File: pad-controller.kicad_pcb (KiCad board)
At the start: 2 copper layers, 14 parts, among them M1 Motor_Servo, M2 Motor_Servo, M3 Motor_Servo, M4 Motor_Servo, SW1 SW_Push_Dual, U2 TPS56121, U3 LD1117S33TR_SOT223

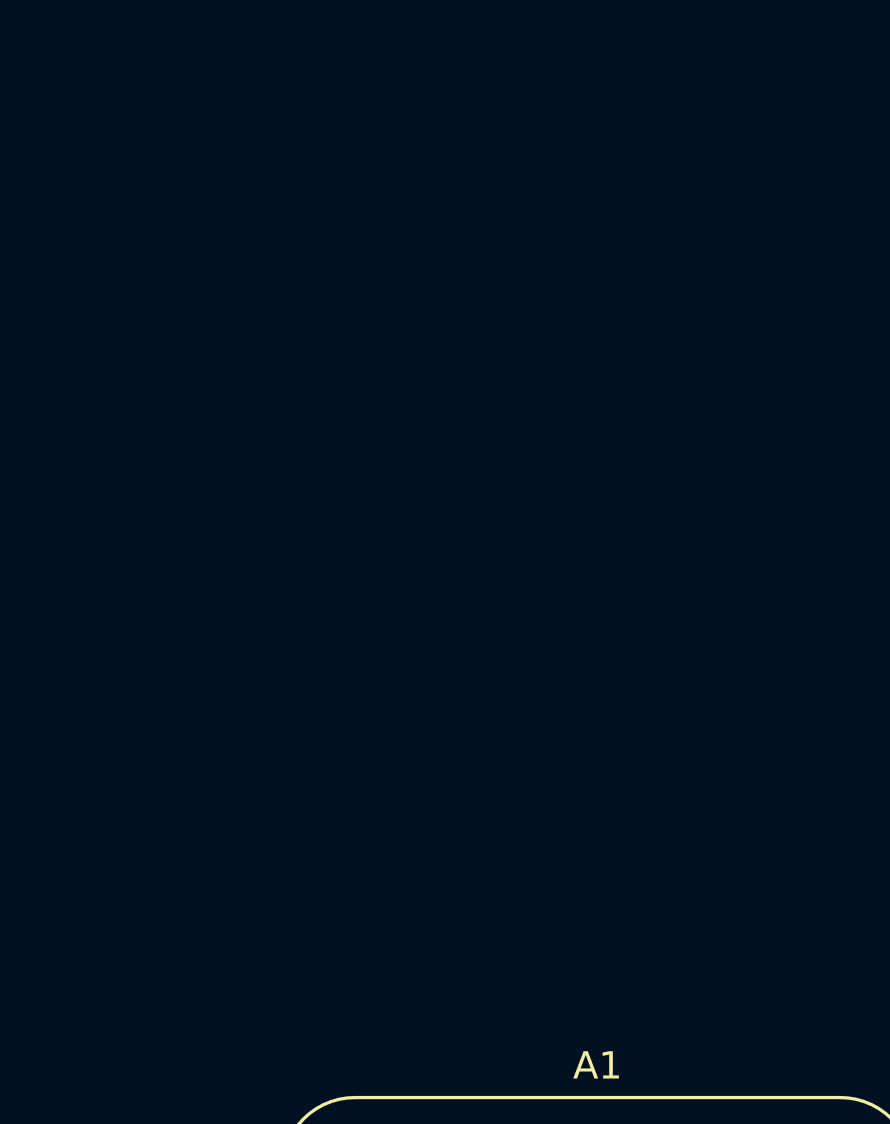
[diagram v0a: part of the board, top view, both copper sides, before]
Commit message: Add XBee footprint
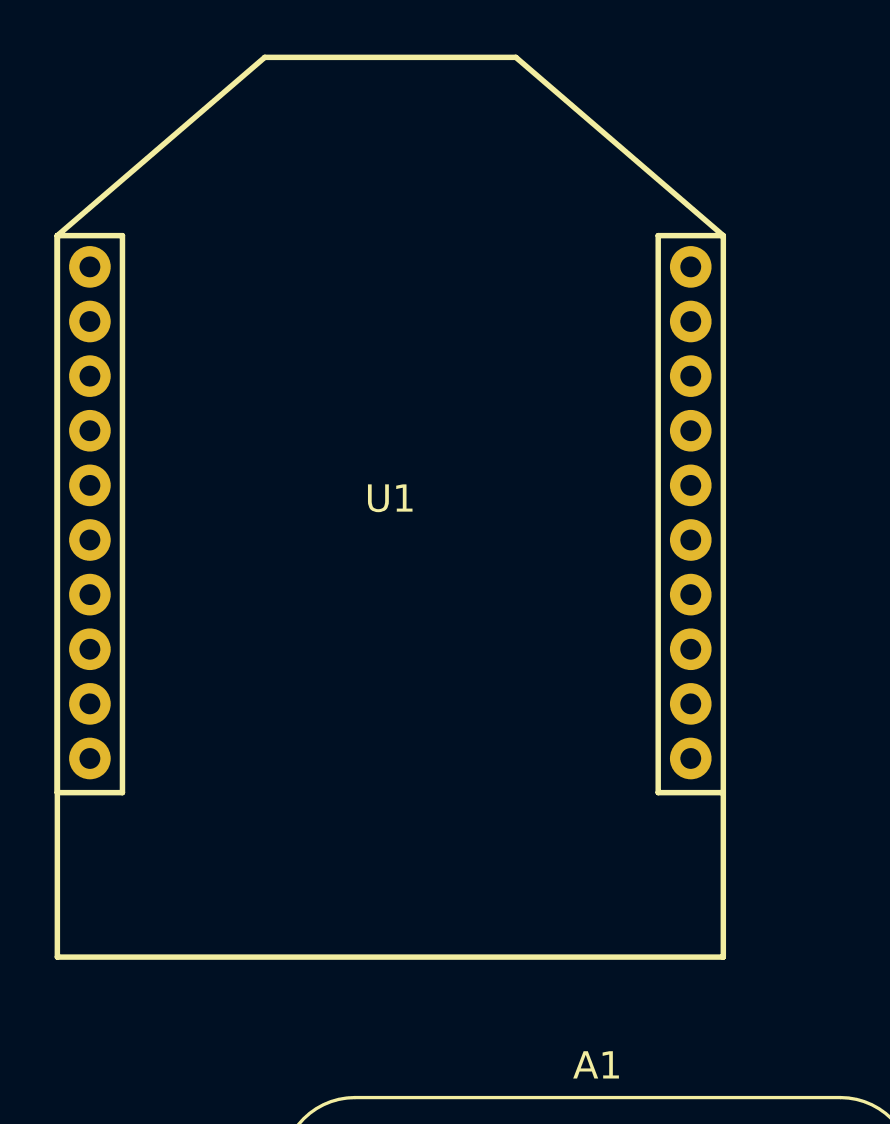
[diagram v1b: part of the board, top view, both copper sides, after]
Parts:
- added U1: Xbee, Marks_Footprints:XBee-PRO 900HP, F.Cu at (65.2, 49.4)
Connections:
- A1 pad 10: unconnected-(A1-A5-Pad10) -> Break Wire
- A1 pad 9: unconnected-(A1-A4-Pad9) -> E-Match
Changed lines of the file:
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@@
   (net 7 "unconnected-(A1-A2-Pad7)")
   (net 8 "unconnected-(A1-A3-Pad8)")
-  (net 9 "unconnected-(A1-A4-Pad9)")
-  (net 10 "unconnected-(A1-A5-Pad10)")
+  (net 9 "E-Match")
+  (net 10 "unconnected-(U1-DIO12{slash}SPI_MISO-Pad4)")
   (net 11 "unconnected-(A1-SCK-Pad11)")
   (net 12 "unconnected-(A1-MOSI-Pad12)")
@@
   (net 41 "Net-(U2-PGOOD)")
   (net 42 "+6V")
+  (net 43 "unconnected-(U1-DIO10{slash}PWM0-Pad6)")
+  (net 44 "unconnected-(U1-DIO11{slash}PWM1-Pad7)")
+  (net 45 "unconnected-(U1-Reserved-Pad8)")
+  (net 46 "unconnected-(U1-DIO4{slash}SPI_MOSI-Pad11)")
+  (net 47 "unconnected-(U1-CTS{slash}DIO7-Pad12)")
+  (net 48 "unconnected-(U1-ON_SLEEP{slash}DIO9-Pad13)")
+  (net 49 "unconnected-(U1-Associate{slash}DIO5-Pad15)")
+  (net 50 "unconnected-(U1-AD3{slash}DIO3{slash}SPI_SSEL-Pad17)")
+  (net 51 "unconnected-(U1-AD2{slash}DIO{slash}SPI_CLK-Pad18)")
+  (net 52 "unconnected-(U1-AD1{slash}DIO1{slash}SPI_ATTN-Pad19)")
+  (net 53 "unconnected-(U1-AD0{slash}DIO0-Pad20)")
   (footprint "Module:Adafruit_Feather" (layer "F.Cu")
     (at 62.63 77.295)
@@
       (net 8 "unconnected-(A1-A3-Pad8)") (pinfunction "A3") (pintype "bidirectional"))
     (pad "9" thru_hole circle (at 0 20.32 180) (size 1.6 1.6) (drill 0.8) (layers "*.Cu" "*.Mask")
-      (net 9 "unconnected-(A1-A4-Pad9)") (pinfunction "A4") (pintype "bidirectional"))
+      (net 9 "E-Match") (pinfunction "A4") (pintype "bidirectional"))
     (pad "10" thru_hole circle (at 0 22.86 180) (size 1.6 1.6) (drill 0.8) (layers "*.Cu" "*.Mask")
-      (net 10 "unconnected-(A1-A5-Pad10)") (pinfunction "A5") (pintype "bidirectional"))
+      (net 23 "Break Wire") (pinfunction "A5") (pintype "bidirectional"))
     (pad "11" thru_hole circle (at 0 25.4 180) (size 1.6 1.6) (drill 0.8) (layers "*.Cu" "*.Mask")
       (net 11 "unconnected-(A1-SCK-Pad11)") (pinfunction "SCK") (pintype "bidirectional"))
@@
     )
   )
+  (footprint "Marks_Footprints:XBee-PRO 900HP" (layer "F.Cu")
+    (at 65.2 49.42)
+    (property "Description" "")
+    (property "Part No." "")
+    (property "Sheetfile" "pad-controller.kicad_sch")
+    (property "Sheetname" "")
+    (attr through_hole)
+    (fp_text reference "U1" (at 0 -0.5 unlocked) (layer "F.SilkS")
+        (effects (font (size 1 1) (thickness 0.1)))
+    )
+    (fp_text value "Xbee" (at 0 1 unlocked) (layer "F.Fab")
+        (effects (font (size 1 1) (thickness 0.15)))
+    )
+    (fp_text user "${REFERENCE}" (at 0 2.5 unlocked) (layer "F.Fab")
+        (effects (font (size 1 1) (thickness 0.15)))
+    )
+    (fp_line (start -12.192 -10.1441) (end -12.192 10.2503)
+      (stroke (width 0.2) (type solid)) (layer "F.SilkS"))
+    (fp_line (start -12.192 -10.1441) (end -9.808 -10.1441)
+      (stroke (width 0.2) (type solid)) (layer "F.SilkS"))
+    (fp_line (start -12.192 -10.1441) (end -4.5974 -16.6719)
+      (stroke (width 0.2) (type solid)) (layer "F.SilkS"))
+    (fp_line (start -12.192 10.2503) (end -9.808 10.2503)
+      (stroke (width 0.2) (type solid)) (layer "F.SilkS"))
+    (fp_line (start -12.192 16.2719) (end -12.192 -10.1441)
+      (stroke (width 0.2) (type solid)) (layer "F.SilkS"))
+    (fp_line (start -12.192 16.2719) (end 12.192 16.2719)
+      (stroke (width 0.2) (type solid)) (layer "F.SilkS"))
+    (fp_line (start -9.808 -10.1441) (end -9.808 10.2503)
+      (stroke (width 0.2) (type solid)) (layer "F.SilkS"))
+    (fp_line (start -4.5974 -16.6719) (end 4.5974 -16.6719)
+      (stroke (width 0.2) (type solid)) (layer "F.SilkS"))
+    (fp_line (start 9.808 -10.1441) (end 9.808 10.2503)
+      (stroke (width 0.2) (type solid)) (layer "F.SilkS"))
+    (fp_line (start 12.192 -10.1441) (end 4.5974 -16.6719)
+      (stroke (width 0.2) (type solid)) (layer "F.SilkS"))
+    (fp_line (start 12.192 -10.1441) (end 9.808 -10.1441)
+      (stroke (width 0.2) (type solid)) (layer "F.SilkS"))
+    (fp_line (start 12.192 10.2503) (end 9.808 10.2503)
+      (stroke (width 0.2) (type solid)) (layer "F.SilkS"))
+    (fp_line (start 12.192 16.2719) (end 12.192 -10.1441)
+      (stroke (width 0.2) (type solid)) (layer "F.SilkS"))
+    (pad "1" thru_hole circle (at -11 -9) (size 1.524 1.524) (drill 0.762) (layers "*.Cu" "*.Mask")
+      (net 2 "+3.3V") (pinfunction "VCC") (pintype "power_in"))
+    (pad "2" thru_hole circle (at -11 -7) (size 1.524 1.524) (drill 0.762) (layers "*.Cu" "*.Mask")
+      (net 14 "MCU RX") (pinfunction "DOUT/DIO13") (pintype "bidirectional"))
+    (pad "3" thru_hole circle (at -11 -5) (size 1.524 1.524) (drill 0.762) (layers "*.Cu" "*.Mask")
+      (net 15 "MCU TX") (pinfunction "DIN/CONFIG/DIO14") (pintype "bidirectional"))
+    (pad "4" thru_hole circle (at -11 -3) (size 1.524 1.524) (drill 0.762) (layers "*.Cu" "*.Mask")
+      (net 10 "unconnected-(U1-DIO12{slash}SPI_MISO-Pad4)") (pinfunction "DIO12/SPI_MISO") (pintype "bidirectional"))
+    (pad "5" thru_hole circle (at -11 -1) (size 1.524 1.524) (drill 0.762) (layers "*.Cu" "*.Mask")
+      (net 29 "/XBee Reset") (pinfunction "RESET") (pintype "input"))
+    (pad "6" thru_hole circle (at -11 1) (size 1.524 1.524) (drill 0.762) (layers "*.Cu" "*.Mask")
+      (net 43 "unconnected-(U1-DIO10{slash}PWM0-Pad6)") (pinfunction "DIO10/PWM0") (pintype "bidirectional"))
+    (pad "7" thru_hole circle (at -11 3) (size 1.524 1.524) (drill 0.762) (layers "*.Cu" "*.Mask")
+      (net 44 "unconnected-(U1-DIO11{slash}PWM1-Pad7)") (pinfunction "DIO11/PWM1") (pintype "bidirectional"))
+    (pad "8" thru_hole circle (at -11 5) (size 1.524 1.524) (drill 0.762) (layers "*.Cu" "*.Mask")
+      (net 45 "unconnected-(U1-Reserved-Pad8)") (pinfunction "Reserved") (pintype "unspecified"))
+    (pad "9" thru_hole circle (at -11 7) (size 1.524 1.524) (drill 0.762) (layers "*.Cu" "*.Mask")
+      (net 25 "XBee DTR") (pinfunction "DTR/SLEEP_RQ/DIO8") (pintype "bidirectional"))
+    (pad "10" thru_hole circle (at -11 9) (size 1.524 1.524) (drill 0.762) (layers "*.Cu" "*.Mask")
+      (net 4 "GND") (pinfunction "GND") (pintype "unspecified"))
+    (pad "11" thru_hole circle (at 11 9 180) (size 1.524 1.524) (drill 0.762) (layers "*.Cu" "*.Mask")
+      (net 46 "unconnected-(U1-DIO4{slash}SPI_MOSI-Pad11)") (pinfunction "DIO4/SPI_MOSI") (pintype "bidirectional"))
+    (pad "12" thru_hole circle (at 11 7 180) (size 1.524 1.524) (drill 0.762) (layers "*.Cu" "*.Mask")
+      (net 47 "unconnected-(U1-CTS{slash}DIO7-Pad12)") (pinfunction "CTS/DIO7") (pintype "bidirectional"))
+    (pad "13" thru_hole circle (at 11 5 180) (size 1.524 1.524) (drill 0.762) (layers "*.Cu" "*.Mask")
+      (net 48 "unconnected-(U1-ON_SLEEP{slash}DIO9-Pad13)") (pinfunction "ON_SLEEP/DIO9") (pintype "bidirectional"))
+    (pad "14" thru_hole circle (at 11 3 180) (size 1.524 1.524) (drill 0.762) (layers "*.Cu" "*.Mask")
+      (net 4 "GND") (pinfunction "VREF") (pintype "unspecified"))
+    (pad "15" thru_hole circle (at 11 1 180) (size 1.524 1.524) (drill 0.762) (layers "*.Cu" "*.Mask")
+      (net 49 "unconnected-(U1-Associate{slash}DIO5-Pad15)") (pinfunction "Associate/DIO5") (pintype "bidirectional"))
+    (pad "16" thru_hole circle (at 11 -1 180) (size 1.524 1.524) (drill 0.762) (layers "*.Cu" "*.Mask")
+      (net 24 "XBee RTS") (pinfunction "RTS/DIO6") (pintype "bidirectional"))
+    (pad "17" thru_hole circle (at 11 -3 180) (size 1.524 1.524) (drill 0.762) (layers "*.Cu" "*.Mask")
+      (net 50 "unconnected-(U1-AD3{slash}DIO3{slash}SPI_SSEL-Pad17)") (pinfunction "AD3/DIO3/SPI_SSEL") (pintype "bidirectional"))
+    (pad "18" thru_hole circle (at 11 -5 180) (size 1.524 1.524) (drill 0.762) (layers "*.Cu" "*.Mask")
+      (net 51 "unconnected-(U1-AD2{slash}DIO{slash}SPI_CLK-Pad18)") (pinfunction "AD2/DIO/SPI_CLK") (pintype "bidirectional"))
+    (pad "19" thru_hole circle (at 11 -7 180) (size 1.524 1.524) (drill 0.762) (layers "*.Cu" "*.Mask")
+      (net 52 "unconnected-(U1-AD1{slash}DIO1{slash}SPI_ATTN-Pad19)") (pinfunction "AD1/DIO1/SPI_ATTN") (pintype "bidirectional"))
+    (pad "20" thru_hole circle (at 11 -9 180) (size 1.524 1.524) (drill 0.762) (layers "*.Cu" "*.Mask")
+      (net 53 "unconnected-(U1-AD0{slash}DIO0-Pad20)") (pinfunction "AD0/DIO0") (pintype "bidirectional"))
+    (group "" (id 0fc5d940-d716-4962-8cde-a77b7cff3545)
+      (members
+        024da15c-26dc-4b55-8604-e4949a14a951
+        1563c857-89c8-482c-9686-303bc2dd3c1f
+        2301c114-c7fa-40ce-8190-09953905d29e
+        2eab3754-36dc-4726-ad37-f4507ae12b77
+        699fe289-da9f-419e-86c8-0cf3e5cf82fd
+        739148f2-d64a-4360-8793-152694a0cd33
+        8bcfc364-4fb2-456e-895f-820d3b1f5813
+        a49b29f1-4b63-41c0-8ca4-9a1434bb2490
+        bd4af66f-2784-42b1-8c44-f6c8c3191e3f
+        ca87e120-d0af-4387-896a-257d27025465
+        d06d0503-951c-4337-8bae-06cf86e1c095
+        da369cd8-a599-4696-806e-536dbfe74ce5
+        edc0558f-42d8-452b-8409-1f884f4bb4d7
+      )
+    )
+  )

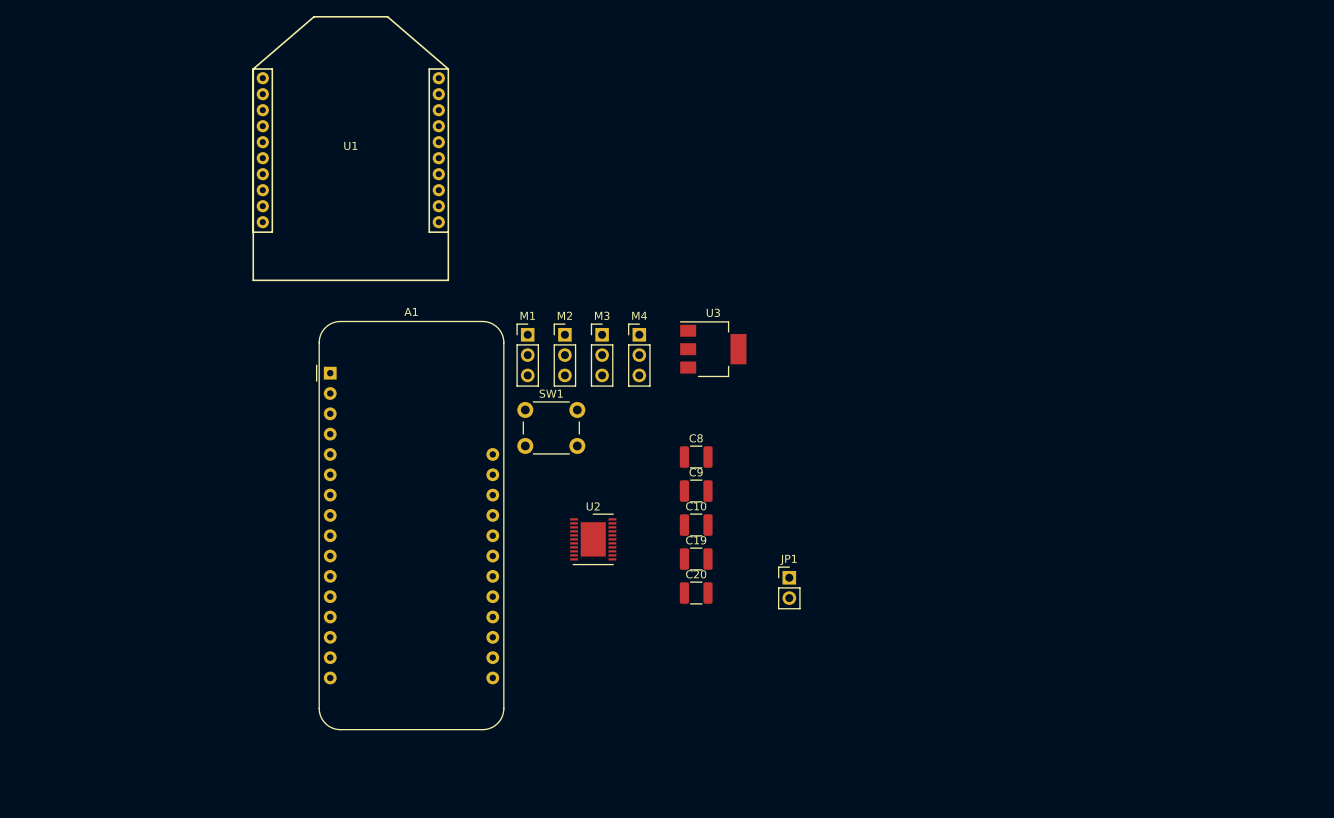
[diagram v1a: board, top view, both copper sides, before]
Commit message: Continue buck converter component selection
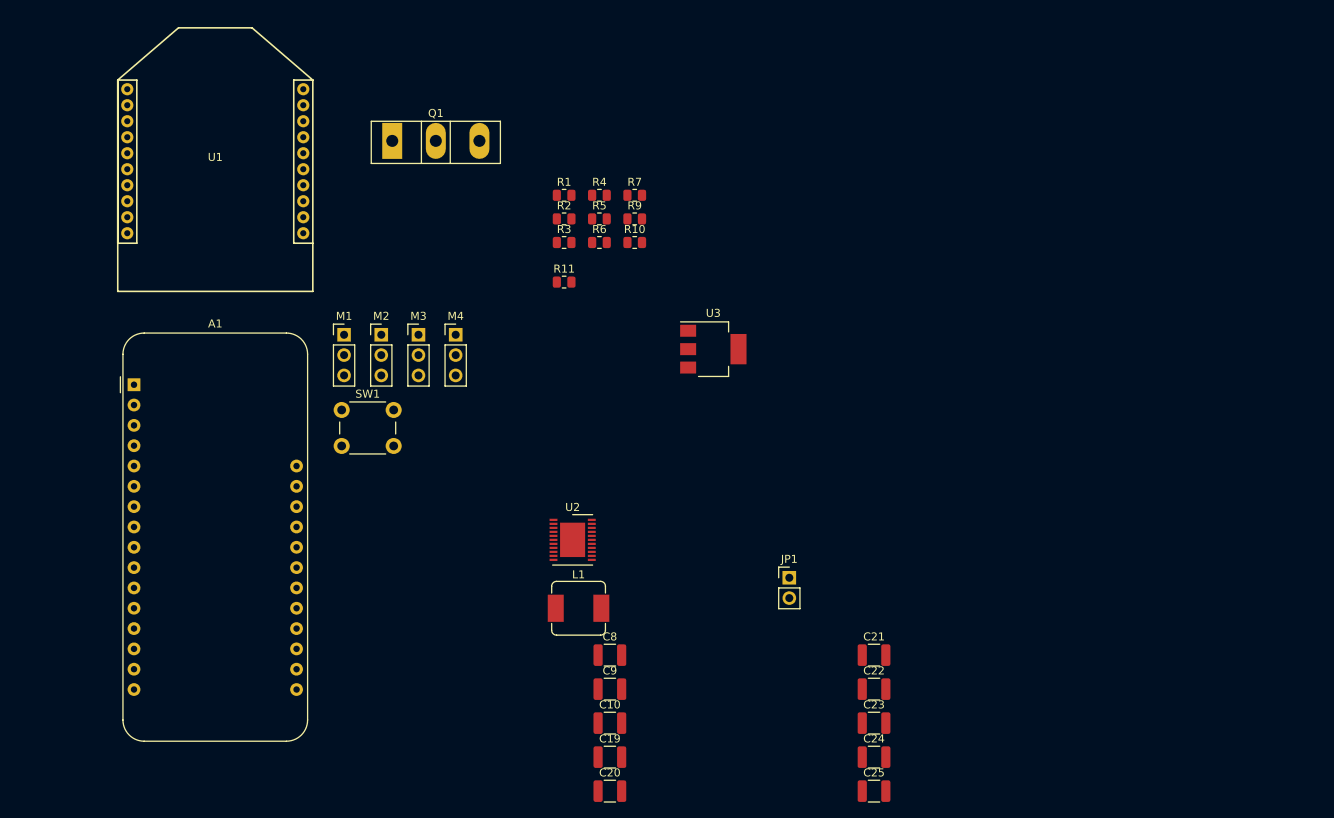
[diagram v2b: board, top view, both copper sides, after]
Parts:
- added C21: 1.0 uF, Capacitor_SMD:C_1210_3225Metric, F.Cu at (130.6, 112.5)
- added C22: 22 uF, Capacitor_SMD:C_1210_3225Metric, F.Cu at (130.6, 116.8)
- added C23: 22 uF, Capacitor_SMD:C_1210_3225Metric, F.Cu at (130.6, 121.0)
- added C24: 22 uF, Capacitor_SMD:C_1210_3225Metric, F.Cu at (130.6, 125.3)
- added C25: 22 uF, Capacitor_SMD:C_1210_3225Metric, F.Cu at (130.6, 129.5)
- added L1: 150 nH, Inductor_SMD:L_Sumida_CDMC6D28_7.25x6.5mm, F.Cu at (93.7, 106.7)
- added Q1: IRFP450PBF, Package_TO_SOT_THT:TO-247-3_Vertical, F.Cu at (70.4, 48.3)
- added R1: 1.78 kΩ, Resistor_SMD:R_0805_2012Metric, F.Cu at (91.9, 55.1)
- added R10: 100 kΩ, Resistor_SMD:R_0805_2012Metric, F.Cu at (100.7, 61.0)
- added R11: R, Resistor_SMD:R_0805_2012Metric, F.Cu at (91.9, 65.9)
- added R2: 5.1 Ω, Resistor_SMD:R_0805_2012Metric, F.Cu at (91.9, 58.0)
- added R3: 442 kΩ, Resistor_SMD:R_0805_2012Metric, F.Cu at (91.9, 61.0)
- added R4: 200 kΩ, Resistor_SMD:R_0805_2012Metric, F.Cu at (96.3, 55.1)
- added R5: 49.9 Ω, Resistor_SMD:R_0805_2012Metric, F.Cu at (96.3, 58.0)
- added R6: 6200 Ω, Resistor_SMD:R_0805_2012Metric, F.Cu at (96.3, 61.0)
- added R7: 22 kΩ, Resistor_SMD:R_0805_2012Metric, F.Cu at (100.7, 55.1)
- added R9: 1.0 Ω, Resistor_SMD:R_0805_2012Metric, F.Cu at (100.7, 58.0)
- moved C10 27.0 mm to (97.6, 121.0)
- moved C19 27.0 mm to (97.6, 125.3)
- moved C8 27.0 mm to (97.6, 112.5)
- moved C9 27.0 mm to (97.6, 116.8)
- moved C20 27.0 mm to (97.6, 129.5)
- moved A1 24.6 mm to (38.1, 78.7)
- moved M1 23.0 mm to (64.4, 72.5)
- moved M2 23.0 mm to (69.0, 72.5)
- moved M3 23.0 mm to (73.7, 72.5)
- moved M4 23.0 mm to (78.3, 72.5)
- moved SW1 23.0 mm to (64.1, 81.9)
- moved U1 17.0 mm to (48.3, 50.8)
- moved U2 2.58 mm to (92.9, 98.1)
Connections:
- net Net-(C14-Pad2) renamed /Power/SW
- U2 pad 20: Net-(U2-VDD) -> +BATT
